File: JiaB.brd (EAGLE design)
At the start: 74.6 x 54 mm, 63 parts, among them J1 STEREO_JACK_SJ-3523, J2 STEREO_JACK_SJ-3523, J3 STEREO_JACK_SJ-3523, J4 STEREO_JACK_SJ-3523

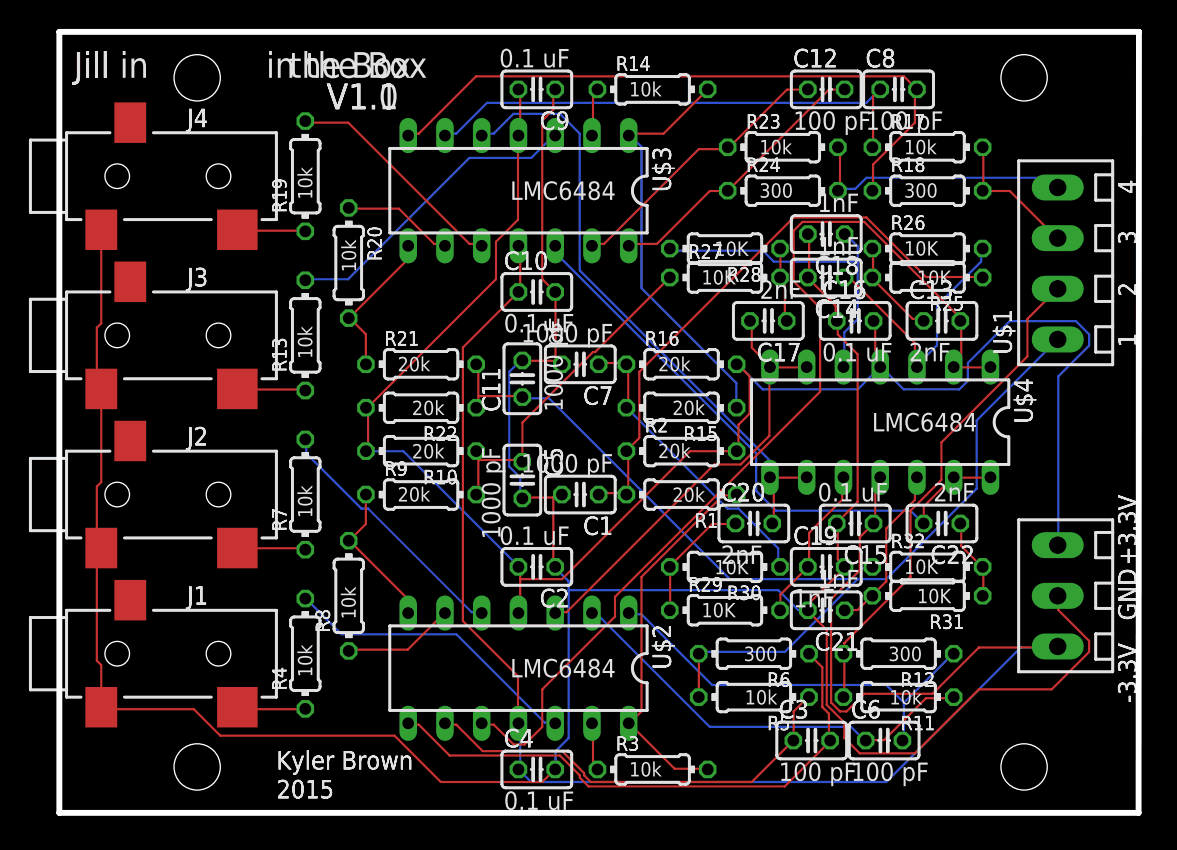
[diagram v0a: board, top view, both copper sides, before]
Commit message: change anti-alias filter component values
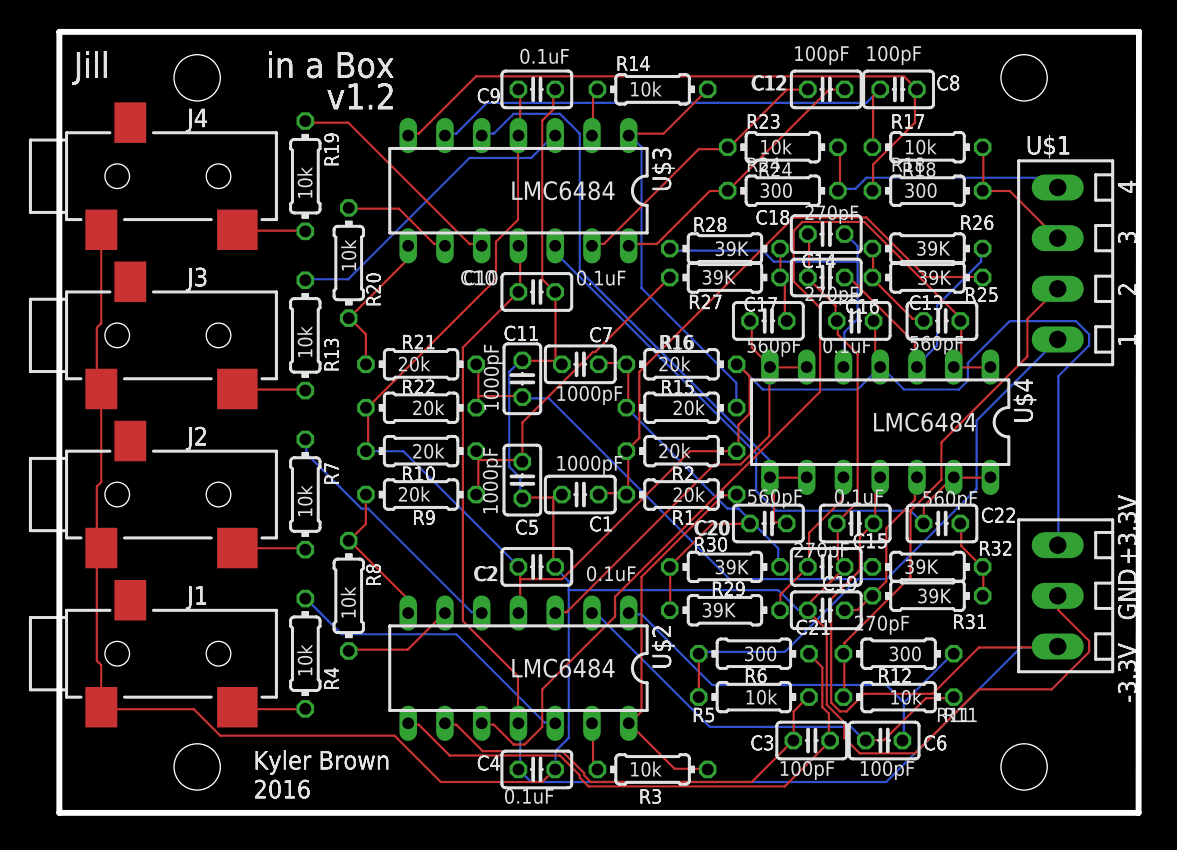
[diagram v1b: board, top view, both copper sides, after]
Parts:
- C1, C11, C5, C7: value 1000 pF -> 1000pF
- C10, C15, C16, C2, C4, C9: value 0.1 uF -> 0.1uF
- C12, C3, C6, C8: value 100 pF -> 100pF
- C13, C17, C20, C22: value 2nF -> 560pF
- C14, C18, C19, C21: value 1nF -> 270pF
- R25, R26, R27, R28, R29, R30, R31, R32: value 10K -> 39K
- moved C20 1.00 mm to (49.0, 20.0)
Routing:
- net N$40: track 8.88 -> 10.7 mm
- net N$41: track 43.2 -> 43.9 mm
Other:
- board text added: "0.1uF"
- board text added: "1000pF"
- board text added: "100pF"
- board text added: "2016"
- board text added: "270pF"
- board text added: "39K"
- board text added: "560pF"
- board text added: "in a Box"
- board text added: "v1.2"
- board text removed: "0.1 uF"
- board text removed: "100 pF"
- board text removed: "1000 pF"
- board text removed: "10K"
- board text removed: "1nF"
- board text removed: "2015"
- board text removed: "2nF"
- board text removed: "Jill in"
- board text removed: "V1.0"
- board text removed: "V1.1"
- board text removed: "in the Box"
- board text removed: "the Box"
